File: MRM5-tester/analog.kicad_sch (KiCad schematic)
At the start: 4 parts, among them IC3 OPA567AIRHGT, T1 ZMPT107-1

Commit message: tester updated 회로도 제작중
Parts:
- added IC1: OPA567AIRHGT, QFN100P500X500X100-13N-D, symbol Mouser:OPA567AIRHGT
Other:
- moved on the sheet: T1
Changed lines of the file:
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@@
 	(symbol
 		(lib_id "Mouser:ZMPT107-1")
-		(at 151.13 53.34 0)
+		(at 39.37 40.64 0)
 		(unit 1)
 		(exclude_from_sim no)
@@
 		(fields_autoplaced yes)
 		(property "Reference" "T1"
-			(at 161.29 45.72 0)
+			(at 49.53 33.02 0)
 			(effects
 				(font
@@
 		)
 		(property "Value" "ZMPT107-1"
-			(at 161.29 48.26 0)
+			(at 49.53 35.56 0)
 			(effects
 				(font
@@
 		)
 		(property "Footprint" "ZMPT1071"
-			(at 167.64 50.8 0)
+			(at 55.88 38.1 0)
 			(effects
 				(font
@@
 		)
 		(property "Datasheet" "https://item.szlcsc.com/136467.html"
-			(at 167.64 53.34 0)
+			(at 55.88 40.64 0)
 			(effects
 				(font
@@
 		)
 		(property "Description" "2mA Voltage transformer 1:1 2mA Plugin Current Sense Transformers ROHS"
-			(at 151.13 53.34 0)
+			(at 39.37 40.64 0)
 			(effects
 				(font
@@
 		)
 		(property "Description_1" "2mA Voltage transformer 1:1 2mA Plugin Current Sense Transformers ROHS"
-			(at 167.64 55.88 0)
+			(at 55.88 43.18 0)
 			(effects
 				(font
@@
 		)
 		(property "Height" "18.4"
-			(at 167.64 58.42 0)
+			(at 55.88 45.72 0)
 			(effects
 				(font
@@
 		)
 		(property "Manufacturer_Name" "Qingxian Zeming Langxi Electronic"
-			(at 167.64 60.96 0)
+			(at 55.88 48.26 0)
 			(effects
 				(font
@@
 		)
 		(property "Manufacturer_Part_Number" "ZMPT107-1"
-			(at 167.64 63.5 0)
+			(at 55.88 50.8 0)
 			(effects
 				(font
@@
 		)
 		(property "Mouser Part Number" ""
-			(at 167.64 66.04 0)
+			(at 55.88 53.34 0)
 			(effects
 				(font
@@
 		)
 		(property "Mouser Price/Stock" ""
-			(at 167.64 68.58 0)
+			(at 55.88 55.88 0)
 			(effects
 				(font
@@
 		)
 		(property "Arrow Part Number" ""
-			(at 167.64 71.12 0)
+			(at 55.88 58.42 0)
 			(effects
 				(font
@@
 		)
 		(property "Arrow Price/Stock" ""
-			(at 167.64 73.66 0)
+			(at 55.88 60.96 0)
 			(effects
 				(font
@@
 					(unit 1)
 				)
+			)
+		)
+	)
+	(symbol
+		(lib_id "Mouser:OPA567AIRHGT")
+		(at 132.08 46.99 0)
+		(unit 1)
+		(exclude_from_sim no)
+		(in_bom yes)
+		(on_board yes)
+		(dnp no)
+		(fields_autoplaced yes)
+		(property "Reference" "IC1"
+			(at 161.29 39.4014 0)
+			(effects
+				(font
+					(size 1.27 1.27)
+				)
+			)
+		)
+		(property "Value" "OPA567AIRHGT"
+			(at 161.29 41.9414 0)
+			(effects
+				(font
+					(size 1.27 1.27)
+				)
+			)
+		)
+		(property "Footprint" "QFN100P500X500X100-13N-D"
+			(at 127.508 72.644 0)
+			(effects
+				(font
+					(size 1.27 1.27)
+				)
+				(justify left)
+				(hide yes)
+			)
+		)
+		(property "Datasheet" "https://www.ti.com/lit/gpn/OPA567"
+			(at 127.508 75.184 0)
+			(effects
+				(font
+					(size 1.27 1.27)
+				)
+				(justify left)
+				(hide yes)
+			)
+		)
+		(property "Description" "Rail-to-Rail I/O, 2A Power Amplifier"
+			(at 160.782 38.1 0)
+			(effects
+				(font
+					(size 1.27 1.27)
+				)
+				(hide yes)
+			)
+		)
+		(property "Description_1" "Rail-to-Rail I/O, 2A Power Amplifier"
+			(at 127.508 77.724 0)
+			(effects
+				(font
+					(size 1.27 1.27)
+				)
+				(justify left)
+				(hide yes)
+			)
+		)
+		(property "Height" "1"
+			(at 127.508 80.264 0)
+			(effects
+				(font
+					(size 1.27 1.27)
+				)
+				(justify left)
+				(hide yes)
+			)
+		)
+		(property "Manufacturer_Name" "Texas Instruments"
+			(at 127.508 82.804 0)
+			(effects
+				(font
+					(size 1.27 1.27)
+				)
+				(justify left)
+				(hide yes)
+			)
+		)
+		(property "Manufacturer_Part_Number" "OPA567AIRHGT"
+			(at 127.508 85.344 0)
+			(effects
+				(font
+					(size 1.27 1.27)
+				)
+				(justify left)
+				(hide yes)
+			)
+		)
+		(property "Mouser Part Number" "595-OPA567AIRHGT"
+			(at 127.508 87.884 0)
+			(effects
+				(font
+					(size 1.27 1.27)
+				)
+				(justify left)
+				(hide yes)
+			)
+		)
+		(property "Mouser Price/Stock" "https://www.mouser.co.uk/ProductDetail/Texas-Instruments/OPA567AIRHGT?qs=wgAEGBTxy7luCwhsvvAe8A%3D%3D"
+			(at 127.508 90.424 0)
+			(effects
+				(font
+					(size 1.27 1.27)
+				)
+				(justify left)
+				(hide yes)
+			)
+		)
+		(property "Arrow Part Number" "OPA567AIRHGT"
+			(at 127.508 92.964 0)
+			(effects
+				(font
+					(size 1.27 1.27)
+				)
+				(justify left)
+				(hide yes)
+			)
+		)
+		(property "Arrow Price/Stock" "https://www.arrow.com/en/products/opa567airhgt/texas-instruments?region=nac"
+			(at 127.508 95.504 0)
+			(effects
+				(font
+					(size 1.27 1.27)
+				)
+				(justify left)
+				(hide yes)
+			)
+		)
+		(pin "8"
+		)
+		(pin "5"
+		)
+		(pin "4"
+		)
+		(pin "13"
+		)
+		(pin "3"
+		)
+		(pin "9"
+		)
+		(pin "12"
+		)
+		(pin "1"
+		)
+		(pin "2"
+		)
+		(pin "11"
+		)
+		(pin "6"
+		)
+		(pin "7"
+		)
+		(pin "10"
+		)
+		(instances
+			(project "MRM5-tester"
+				(path "/6e775c75-0b09-4e5f-9bff-c5585ac94ad7/d46285ed-39e7-481d-bc83-4a7d1879f6d2"
+					(reference "IC1")
+					(unit 1)
+				)

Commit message: tester PCB 작성중
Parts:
- removed IC1: OPA567AIRHGT, QFN100P500X500X100-13N-D, symbol Mouser:OPA567AIRHGT
- removed R9: NSP500JB-3R3, PCM_Resistor_THT_US_AKL:R_Axial_DIN0918_L18.0mm_D9.0mm_P22.86mm_Horizontal, symbol PCM_Resistor_US_AKL:R_DIN0918_P22.86mm
- added C10, C9: 100n, PCM_Capacitor_SMD_AKL:C_0402_1005Metric, symbol PCM_Capacitor_AKL:C_0402
- added C11, C13: 15n, PCM_Capacitor_SMD_AKL:C_0402_1005Metric, symbol PCM_Capacitor_AKL:C_0402
- added C12, C8: 47u, PCM_Capacitor_SMD_AKL:C_0603_1608Metric, symbol PCM_Capacitor_AKL:C_0603
- added C14: 82n, PCM_Capacitor_SMD_AKL:C_0402_1005Metric, symbol PCM_Capacitor_AKL:C_0402
- added C7: 10n, PCM_Capacitor_SMD_AKL:C_0402_1005Metric, symbol PCM_Capacitor_AKL:C_0402
- added P3, P4: ~, Mouser:PAD_Hole_D2mm, symbol Mouser:PAD_hole2.6
- added R15: MBB02070C1004FCT00, Mouser:RESAD1650W60L650D250, symbol ktw07182:MBB02070C1004FCT00
- added R16: 4.64k, PCM_Resistor_SMD_AKL:R_0402_1005Metric, symbol PCM_Resistor_AKL:R_0402
- added R17: 12.7k, PCM_Resistor_SMD_AKL:R_0402_1005Metric, symbol PCM_Resistor_AKL:R_0402
- added R18: 16.2k, PCM_Resistor_SMD_AKL:R_0402_1005Metric, symbol PCM_Resistor_AKL:R_0402
- added R20: 2.37k, PCM_Resistor_SMD_AKL:R_0402_1005Metric, symbol PCM_Resistor_AKL:R_0402
- added R21: 4.99k, PCM_Resistor_SMD_AKL:R_0402_1005Metric, symbol PCM_Resistor_AKL:R_0402
- added R22: 3.3, PCM_Resistor_THT_US_AKL:R_Axial_DIN0918_L18.0mm_D9.0mm_P22.86mm_Horizontal, symbol PCM_Resistor_US_AKL:R_DIN0918_P22.86mm
- added TP1: Vf, TestPoint:TestPoint_Pad_D2.0mm, symbol Connector:TestPoint
- added TP2: V1, TestPoint:TestPoint_Pad_D2.0mm, symbol Connector:TestPoint
- added U2: ADA4528-2ACPZ, PCM_Package_DFN_QFN_AKL:DFN-8-1EP_3x3mm_P0.5mm_EP1.66x2.38mm, symbol PCM_Amplifier_Operational_AKL:ADA4528-2ACPZ
- IC2: renamed from IC3; footprint QFN100P500X500X100-13N-D -> Mouser:QFN100P500X500X100-13N-D
- T1: footprint ZMPT1071 -> Mouser:ZMPT1071
- renumbered R10 to R19
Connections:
- net 3V3: now reaches IC2.1 (V+_1)
- net 3V3: now also IC2.12 (V+_2), C10.2, C12.1, U2.8 (V+)
- net Z_TFlag: now reaches IC2.10 (TFLAG)
- net Z_TFlag: now also IC2.11 (ENABLE)
- net 1V6: now reaches IC2.13 (EP)
- net 1V6: now also T1.4, C10.1, C12.2, C13.1, C7.1, C8.2, C9.1, P4.1, R16.1, U2.9 (PAD)
- net at IC2.2 (V_O_1): now also IC2.3 (V_O_2), IC2.8 (-IN), R22.1
- net GND: now reaches IC2.4 (V-_1)
- net GND: now also IC2.5 (V-_2), R19.1, C8.1, C9.2, U2.4 (V-)
- net at IC2.6 (ISET): now also R19.2
- net Z_IFlag: now reaches IC2.7 (IFLAG)
- net sigZ: now reaches IC2.9 (+IN)
- net at T1.1: now also R15.2
- net Vn_h: now reaches T1.2
- net at T1.3: now also R16.2, R17.1
- new net: P3.1, R22.2
- new net: C11.2, R20.1, TP1.1, U2.1, U2.2 (-)
- new net: C7.2, R18.2, U2.3 (+)
- new net: C14.1, R20.2, R21.1
- new net: C13.2, R21.2, U2.5 (+)
- new net: C11.1, R17.2, R18.1
- new net Vp_sh: R15.1
- new net sigV: C14.2, TP2.1, U2.6 (-), U2.7
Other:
- moved on the sheet: IC2, R19

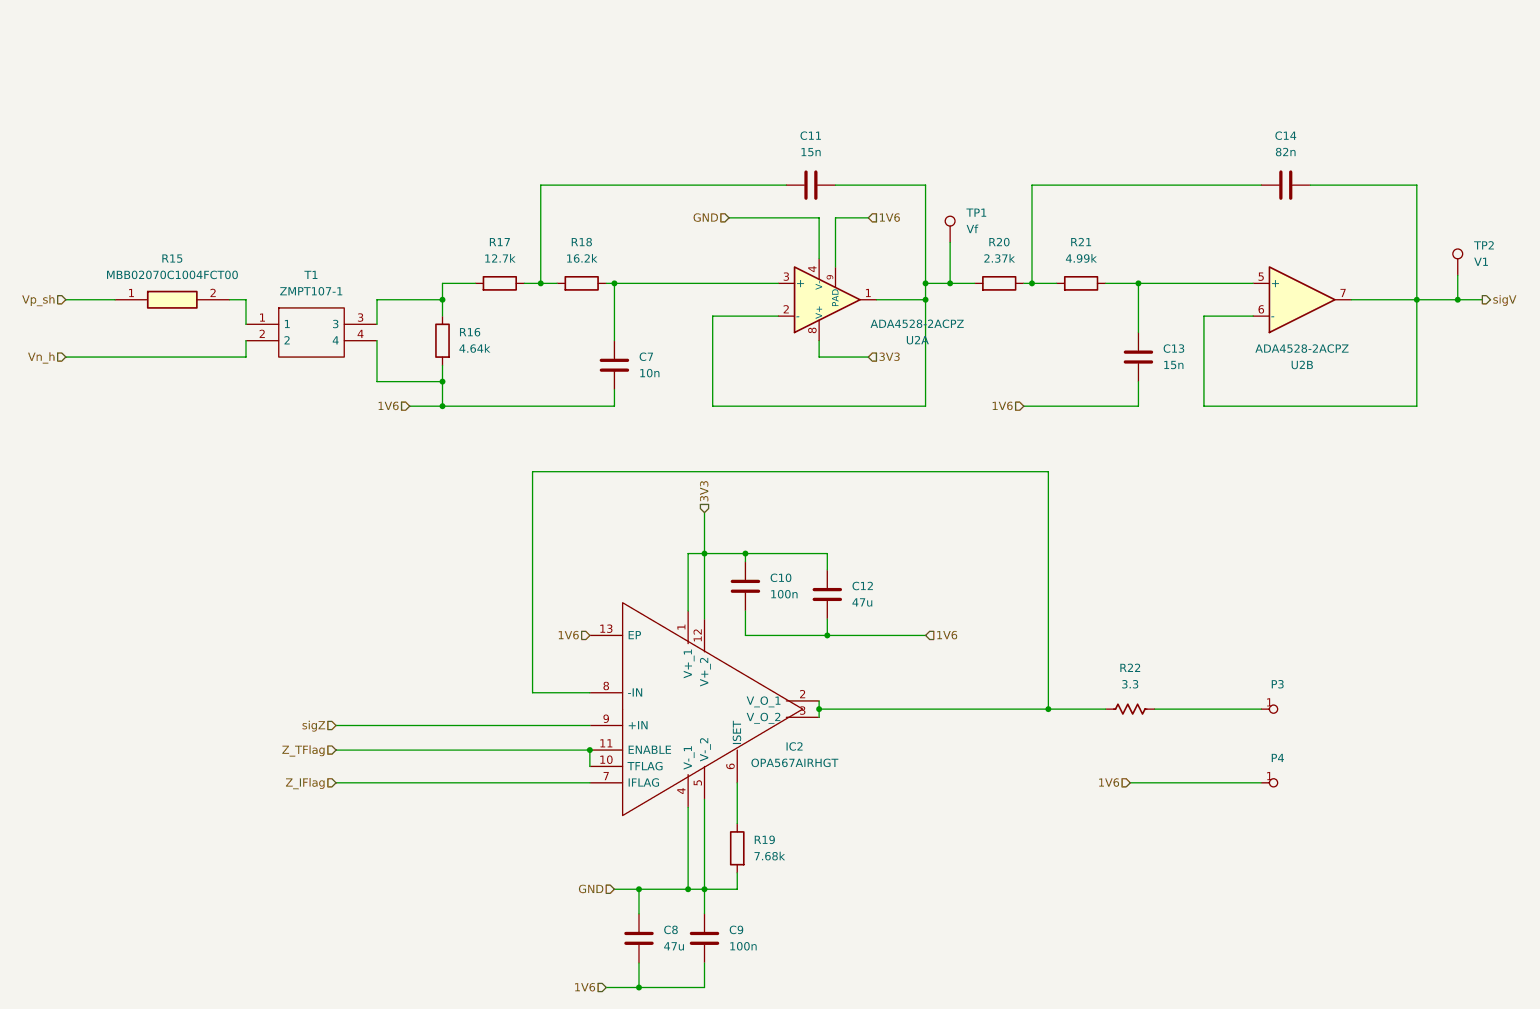
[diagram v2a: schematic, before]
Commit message: tester pcb 디자인 완료
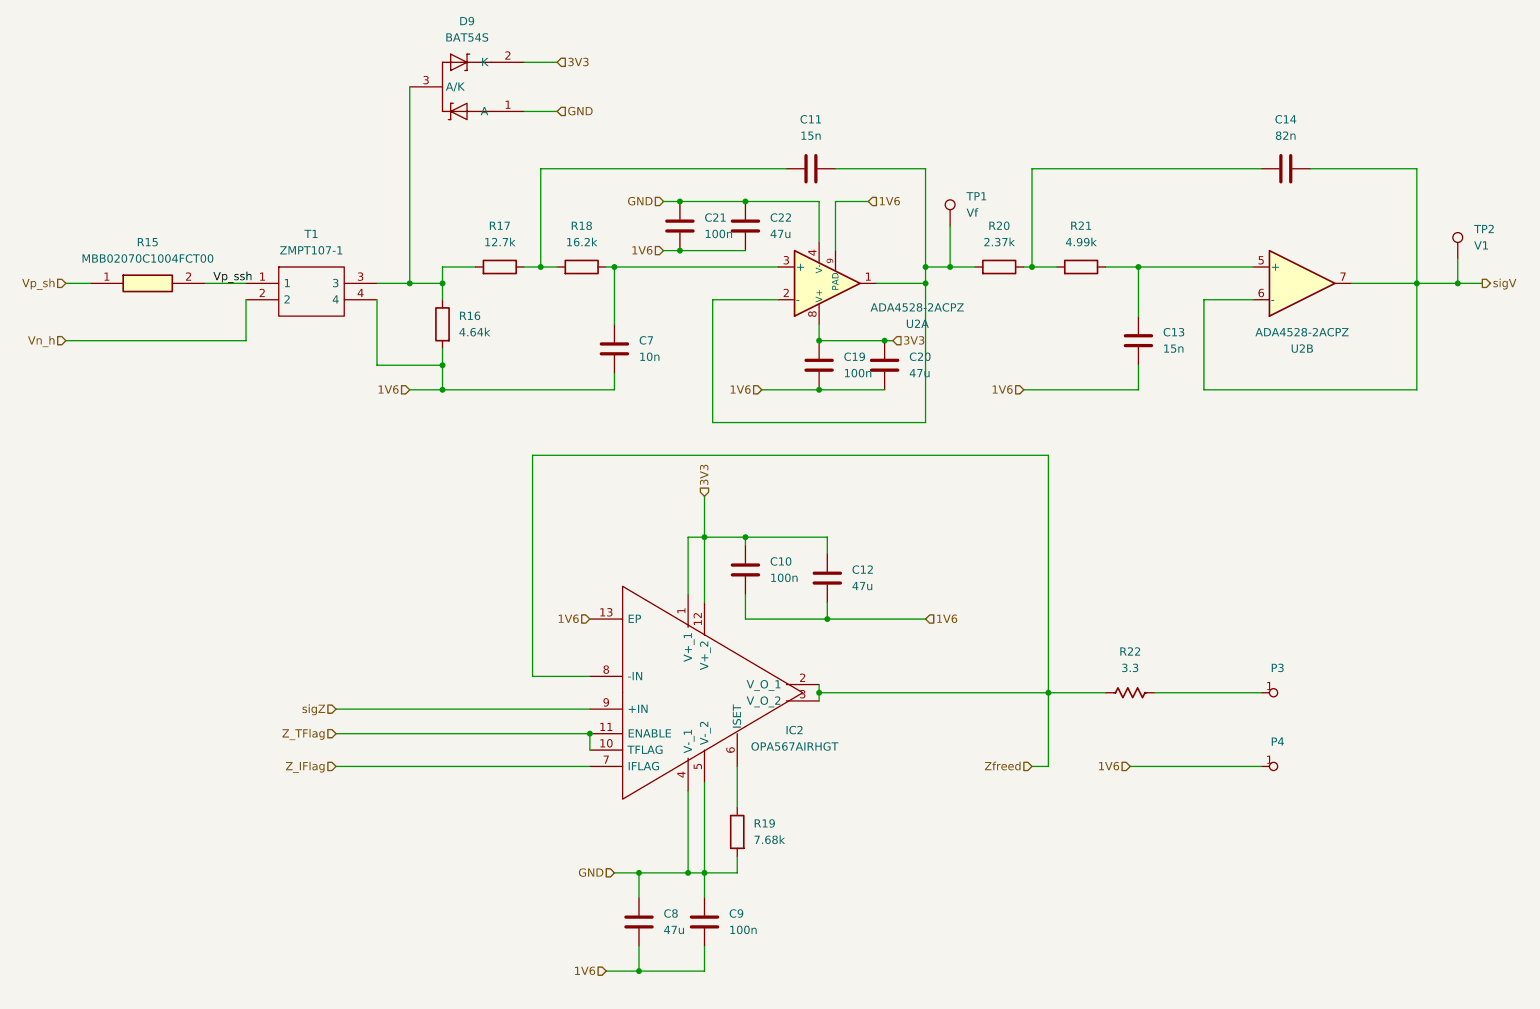
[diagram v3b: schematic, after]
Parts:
- added C19, C21: 100n, PCM_Capacitor_SMD_AKL:C_0402_1005Metric, symbol PCM_Capacitor_AKL:C_0402
- added C20, C22: 47u, PCM_Capacitor_SMD_AKL:C_0603_1608Metric, symbol PCM_Capacitor_AKL:C_0603
- added D9: BAT54S, SOT95P240X120-3N, symbol ktw07182:BAT54S
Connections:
- net 1V6: now also C19.1, C20.2, C21.1, C22.2
- net 3V3: now also C19.2, C20.1, D9.2 (K)
- net GND: now also C21.2, C22.1, D9.1 (A)
- net Zfreed: now reaches IC2.2 (V_O_1), IC2.3 (V_O_2), IC2.8 (-IN), R22.1
- net at R16.2, R17.1, T1.3: now also D9.3 (A/K)
- net Vp_ssh: now reaches R15.2, T1.1
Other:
- moved on the sheet: C10, C11, C12, C13, C14, C7, C8, C9, IC2, P3, P4, R15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

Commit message: tester PCB 검토
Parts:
- added TP3: Z, TestPoint:TestPoint_Pad_D2.0mm, symbol Connector:TestPoint
- TP2: value V1 -> V
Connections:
- net Zfreed: now also TP3.1
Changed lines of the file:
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@@
+	)
+	(junction
+		(at 190.5 139.7)
+		(diameter 0)
+		(color 0 0 0 0)
 	)
 	(junction
@@
 		(pts
 			(xy 148.59 67.31) (xy 138.43 67.31)
+		)
+		(stroke
+			(width 0)
+			(type default)
+		)
+	)
+	(wire
+		(pts
+			(xy 190.5 139.7) (xy 190.5 144.78)
 		)
 		(stroke
@@
 			)
 		)
-		(property "Value" "V1"
+		(property "Value" "V"
 			(at 256.54 58.9279 0)
 			(effects
@@
 					(unit 1)
 				)
+			)
+		)
+	)
+	(symbol
+		(lib_id "Connector:TestPoint")
+		(at 190.5 144.78 180)
+		(unit 1)
+		(exclude_from_sim no)
+		(in_bom yes)
+		(on_board yes)
+		(dnp no)
+		(fields_autoplaced yes)
+		(property "Reference" "TP3"
+			(at 193.04 146.8119 0)
+			(effects
+				(font
+					(size 1.27 1.27)
+				)
+				(justify right)
+			)
+		)
+		(property "Value" "Z"
+			(at 193.04 149.3519 0)
+			(effects
+				(font
+					(size 1.27 1.27)
+				)
+				(justify right)
+			)
+		)
+		(property "Footprint" "TestPoint:TestPoint_Pad_D2.0mm"
+			(at 185.42 144.78 0)
+			(effects
+				(font
+					(size 1.27 1.27)
+				)
+				(hide yes)
+			)
+		)
+		(property "Datasheet" "~"
+			(at 185.42 144.78 0)
+			(effects
+				(font
+					(size 1.27 1.27)
+				)
+				(hide yes)
+			)
+		)
+		(property "Description" "test point"
+			(at 190.5 144.78 0)
+			(effects
+				(font
+					(size 1.27 1.27)
+				)
+				(hide yes)
+			)
+		)
+		(pin "1"
+		)
+		(instances
+			(project "MRM5-tester"
+				(path "/6e775c75-0b09-4e5f-9bff-c5585ac94ad7/d46285ed-39e7-481d-bc83-4a7d1879f6d2"
+					(reference "TP3")
+					(unit 1)
+				)
